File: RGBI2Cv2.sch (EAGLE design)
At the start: 10 parts, among them Q1 STP16NF06, Q2 STP16NF06, Q3 STP16NF06, U2 ATTINY45-20PU

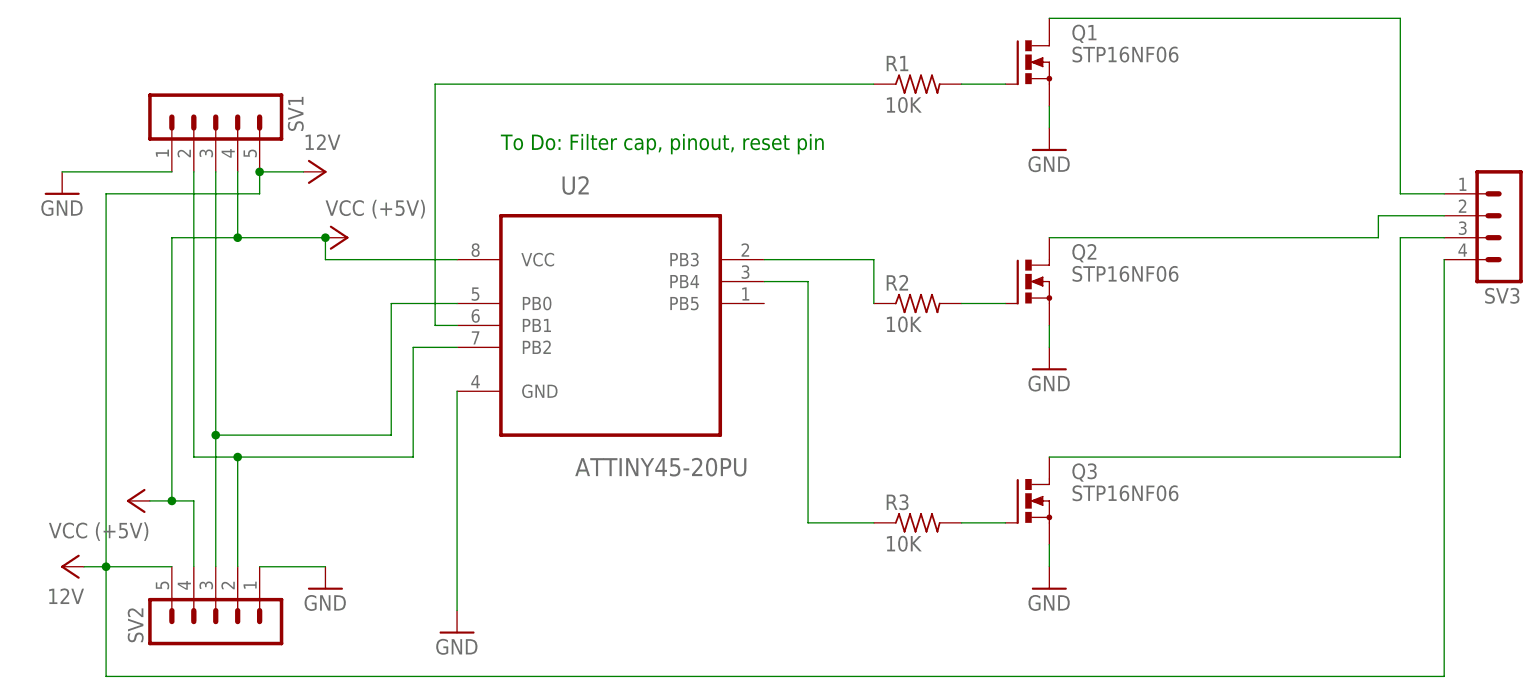
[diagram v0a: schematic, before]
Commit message: Updated design.
Fixed:
Corrected wiring of in/out headers
Corrected net issue to fix 12v/5v mix
Changed resistor symbol

Added:
Filter caps for ATTiny45
Labled components
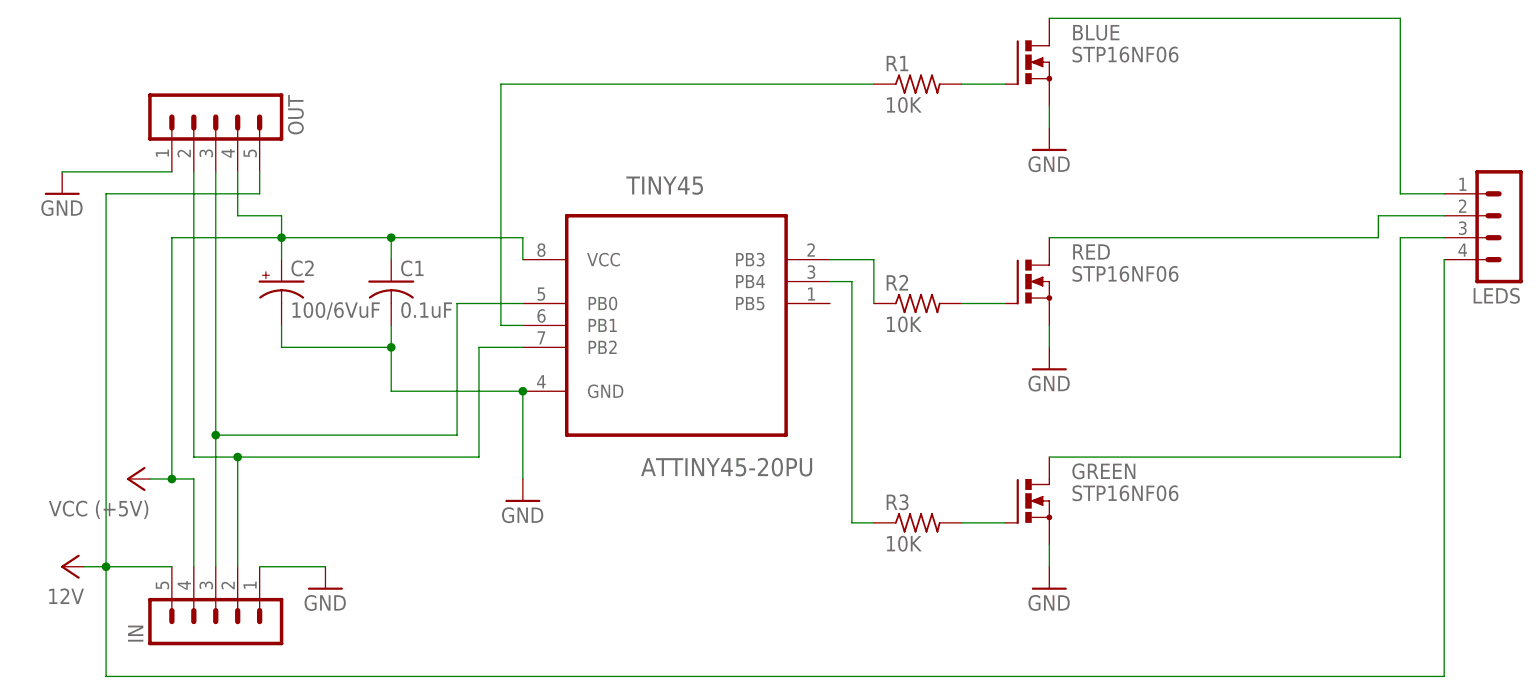
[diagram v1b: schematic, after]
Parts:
- removed U2: ATTINY45-20PU, Atmel_By_element14_Batch_1:ATTINY45-20PU
- added C1: 0.1uF, minimidi:C-US025-025X050
- added C2: 100/6VuF, minimidi:CPOL-USE2.5-6
- added TINY45: ATTINY45-20PU, Atmel_By_element14_Batch_1:ATTINY45-20PU
- R1, R2, R3: device resistor:R-US_0411/15 -> rcl:R-US_0207/7
- renumbered Q1 to BLUE, Q2 to RED, Q3 to GREEN, SV1 to OUT, SV2 to IN, SV3 to LEDS
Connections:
- removed net VCC: IN.4, IN.5, LEDS.4, OUT.4, OUT.5, U2.VCC
- new net 12V: IN.5, LEDS.4, OUT.5
- new net VCC5V: C1.1, C2.+, IN.4, OUT.4, TINY45.VCC
- net GND: now also C1.2, C2.-, TINY45.GND; no longer U2.GND
- net N$10: now also TINY45.PB4; no longer U2.PB4
- net N$3: now also TINY45.PB2; no longer U2.PB2
- net N$4: now also TINY45.PB0; no longer U2.PB0
- net N$5: now also TINY45.PB1; no longer U2.PB1
- net N$9: now also TINY45.PB3; no longer U2.PB3
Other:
- note removed: "To Do: Filter cap, pinout, reset pin"
